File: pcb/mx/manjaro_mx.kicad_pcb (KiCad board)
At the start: 2 copper layers, 286.5 x 113.5 mm, 99 parts, among them J2 MJ-4PP-9, SW1 SW_Push, SW10 SW_Push, SW11 SW_Push, SW12 SW_Push, SW13 SW_Push, SW14 SW_Push, SW15 SW_Push, SW16 SW_Push, SW17 SW_Push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

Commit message: Modify MCU position
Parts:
- moved rU1 107.8 mm to (300.0, 54.0), turned to 180 degrees
- moved U1 106.9 mm to (55.0, 54.0), turned to 0 degrees
- moved BT1 17.0 mm to (139.0, 50.5), turned to 90 degrees
- moved rBT1 15.5 mm to (216.0, 48.5), turned to -90 degrees
- moved rPowerSW1 13.0 mm to (232.1, 48.5)
- moved PowerSW1 11.2 mm to (125.0, 48.5)
- moved D19 2.00 mm to (164.5, 144.5)
- moved D20 2.00 mm to (145.5, 137.5)
- moved SW19 2.00 mm to (161.2, 138.1)
- moved SW20 2.00 mm to (141.2, 131.1)
- moved rD19 2.00 mm to (191.0, 144.7)
- moved rD20 2.00 mm to (210.0, 137.3)
- moved rSW19 2.00 mm to (194.0, 138.1)
- moved rSW20 2.00 mm to (214.0, 131.1)
- moved J2 1.50 mm to (166.0, 118.0)
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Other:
- board size 286.5 x 113.5 mm -> 286.5 x 118.5 mm

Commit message: Fixed production files
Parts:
- added ?: , , F.Cu at (145.0, 42.5)
- added ?: , , F.Cu at (214.0, 42.5)
- added ?: , , F.Cu at (144.0, 42.5)
- added ?: , , F.Cu at (142.0, 42.5)
- added ?: , , F.Cu at (141.0, 42.5)
- added ?: , , F.Cu at (210.0, 42.5)
- added ?: , , F.Cu at (211.0, 42.5)
- added ?: , , F.Cu at (212.0, 42.5)
- added ?: , , F.Cu at (213.0, 42.5)
- added ?: , , F.Cu at (143.0, 42.5)
- turned rPowerSW1 to 0 degrees
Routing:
- net rBAT-: track 0.00 -> 311.2 mm, vias 0 -> 1
- net rROW3: track 0.00 -> 229.2 mm, vias 0 -> 1
- net ROW3: track 0.00 -> 219.5 mm, vias 0 -> 1
- net BAT-: track 0.00 -> 212.9 mm, vias 0 -> 3
- net ROW2: track 0.00 -> 199.5 mm, vias 0 -> 1
- net DATA: track 0.00 -> 192.5 mm
- net rROW2: track 0.00 -> 184.7 mm, vias 0 -> 1
- net ROW1: track 0.00 -> 180.6 mm, vias 0 -> 1
- net rDATA: track 0.00 -> 178.1 mm, vias 0 -> 2
- net rVCC: track 0.00 -> 175.2 mm, vias 0 -> 3
- net VCC: track 0.00 -> 174.7 mm
- net COL0: track 0.00 -> 173.9 mm, vias 0 -> 8
- net REB: track 0.00 -> 168.0 mm, vias 0 -> 2
- net rKEYEX1: track 0.00 -> 167.3 mm
- net rCOL0: track 0.00 -> 166.0 mm, vias 0 -> 6
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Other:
- outline, holes or cut-outs redrawn
- board text added: "+"
- board text added: "-"
- board text added: "On"

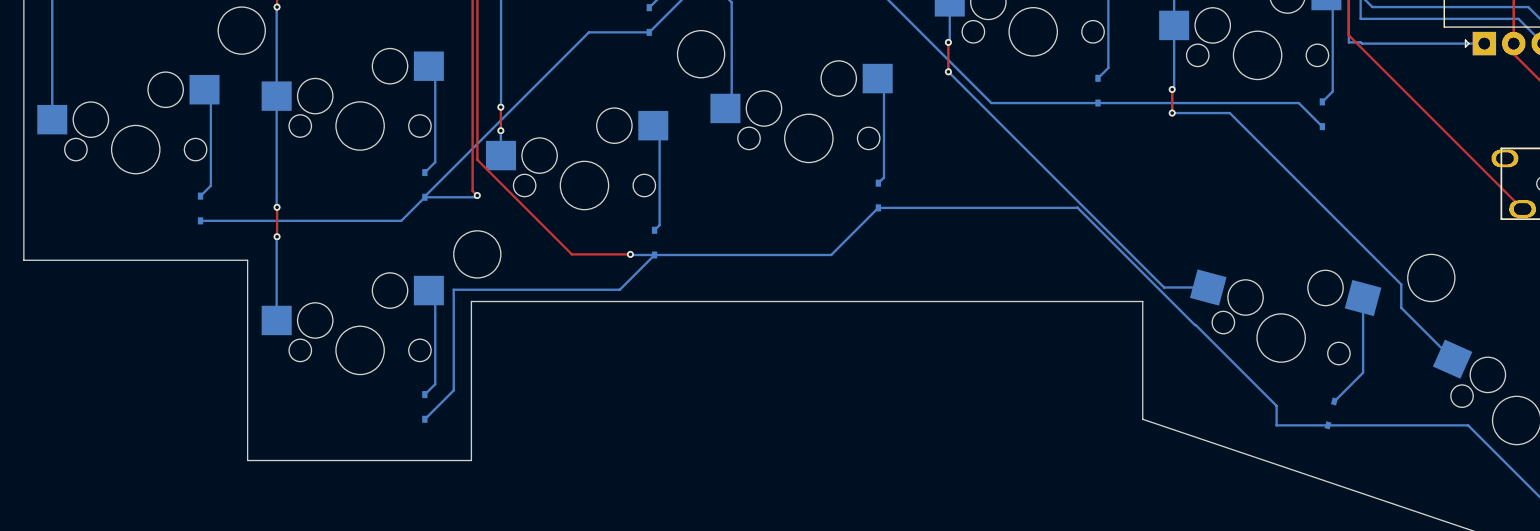
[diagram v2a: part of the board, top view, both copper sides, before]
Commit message: Add 1key on left hand
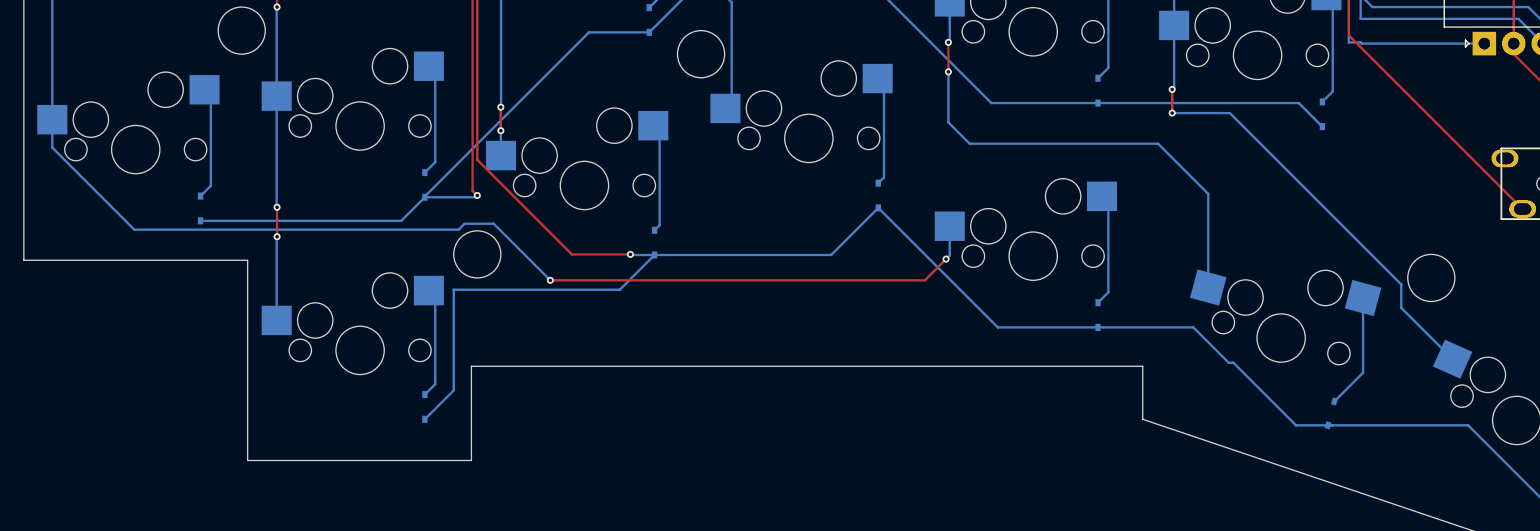
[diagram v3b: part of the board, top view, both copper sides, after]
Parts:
- added D24: 1N4148WT, Keebio-Parts:D_SOD-323, B.Cu at (125.7, 129.2)
- added SW24: SW_Push, kbd:keyswitch_cherrymx_hotswap_1u, B.Cu at (120.2, 124.2)
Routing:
- net COL5: track 76.0 -> 163.0 mm, vias 0 -> 2
- net Net-(D24-A): track 0.00 -> 9.62 mm
- net COL1: track 144.6 -> 151.8 mm
- net ROW3: track 219.5 -> 218.9 mm
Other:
- outline, holes or cut-outs redrawn
